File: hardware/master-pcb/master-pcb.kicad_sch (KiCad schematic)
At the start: 56 parts, among them J1 RS-485 OUT, J2 INT IN 0-8, J4 UNDERGLOW OUT, SW1 PLAYER_ID, U1 Teensy 4.0, U2 THVD1429, U3 SN74AHCT125

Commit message: Harness rework: INT twisted pair on JST XH, RS-485 shield on Micro-Fit pin 3
Two cabling changes, both of which replace earlier decisions.

INT goes twisted pair (signal + dedicated GND return)
-----------------------------------------------------
The panel side needed no change: J9 pin 2 was provisioned as GND for
exactly this on 2026-07-24. On the master, the 9-position pluggable
Euroblock is replaced by nine JST XH 2-pin vertical headers (B2B-XH-A),
placed as J2, J3, J5-J11 -- non-contiguous because renumbering J4 would
churn the docs for no gain.

Nine discrete 5.08mm screw blocks were rejected outright: ~92mm of board
edge against a 77.5mm board. XH is top-entry, so it needs no board edge
at all and the nine fit in roughly what the Euroblock vacated (~42x13.5
vs 45.72x12.0mm). XH is also keyed, so signal and GND cannot be swapped
at assembly -- that swap on a screw terminal ties INT to GND and reads as
a permanently stuck press. Keeping XH here while panel FSRs stay PH also
means an FSR lead cannot be plugged into an INT header.

Cost accepted: nine plugs instead of one detachable block.

Connectors are silkscreened by panel position (UL/U/UR/L/C/R/DL/D/DR),
left to right in panel order 0->8. This supersedes the old "J2 position 1
is panel 8" reversal note -- the mapping is now monotonic.

RS-485 shield terminated on pin 3
---------------------------------
Reverses the 2026-07-24 "drain floating at both ends" decision. That
reasoning was sound on its own terms; this takes the upgrade path the
old note itself described as a five-minute change.

Hybrid grounding, one continuous shield master -> panel 8:
  - master J1 pin 3 -> GND, the single DC reference for the network
  - each panel: RS485_Shield passes J8.3 -> J10.3, no local GND tie,
    plus C57 100nF || R20 1M to GND near J8

The per-panel caps are not decoration: ~6-8m of foil grounded at one end
only resonates near 10MHz, inside 1Mbps harmonic content. The cap grounds
it at RF while blocking DC, so no loo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
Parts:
- removed J2: INT IN 0-8, master-pcb:TerminalBlock_Molex_39531_1x09_P5.08mm_Vertical, symbol Connector_Generic:Conn_01x09
- added J10, J11, J2, J3, J5, J6, J7, J8, J9: B2B-XH-A, Connector_JST:JST_XH_B2B-XH-A_1x02_P2.50mm_Vertical, symbol Connector_Generic:Conn_01x02
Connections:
- net GND: now also J1.3 (Pin_3), J10.2 (Pin_2), J11.2 (Pin_2), J2.2 (Pin_2), J3.2 (Pin_2), J5.2 (Pin_2), J6.2 (Pin_2), J7.2 (Pin_2), J8.2 (Pin_2), J9.2 (Pin_2)
- net at D4.1 (K), R8.1: now also J5.1 (Pin_1)
- net at D2.1 (K), R6.1: now also J2.1 (Pin_1)
- net at D3.1 (K), R7.1: now also J3.1 (Pin_1)
- net at D10.1 (K), R14.1: now also J11.1 (Pin_1)
- net at D8.1 (K), R12.1: now also J9.1 (Pin_1)
- net at D5.1 (K), R9.1: now also J6.1 (Pin_1)
- net at D6.1 (K), R10.1: now also J7.1 (Pin_1)
- net at D7.1 (K), R11.1: now also J8.1 (Pin_1)
- net at D9.1 (K), R13.1: now also J10.1 (Pin_1)
- no-connect marks 12 -> 11
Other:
- note added: "*Shield"

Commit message: master: renumber reference designators contiguously from 1
The review conventions ask that each RefDes type start at 1 with no
numeric gaps. This board was missing D1 and R2. Reannotated, then pushed
through to the layout.

DRC 0, unconnected 0, schematic parity 0, ERC 0 with zones refilled.
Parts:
- renumbered C4 to C10, C3 to C11, C11 to C3, C10 to C4, C9 to C5, C8 to C6, C6 to C8, C5 to C9, D10 to D1, D9 to D2, D8 to D3, D7 to D4, D6 to D5, D5 to D6, D4 to D7, D3 to D8, D2 to D9, H3 to H2, H2 to H3, J4 to J2, J2 to J3, J3 to J4, R4 to R1, R9 to R11, R8 to R12, R7 to R13, R6 to R14, R5 to R2, R1 to R3, R15 to R4, R3 to R5, R14 to R6, R13 to R7, R12 to R8, R11 to R9, TP9 to TP1, TP8 to TP10, TP3 to TP2, TP10 to TP3, TP5 to TP4, TP6 to TP5, TP4 to TP6, TP1 to TP7, TP2 to TP8, TP7 to TP9, U2 to U1, U1 to U2

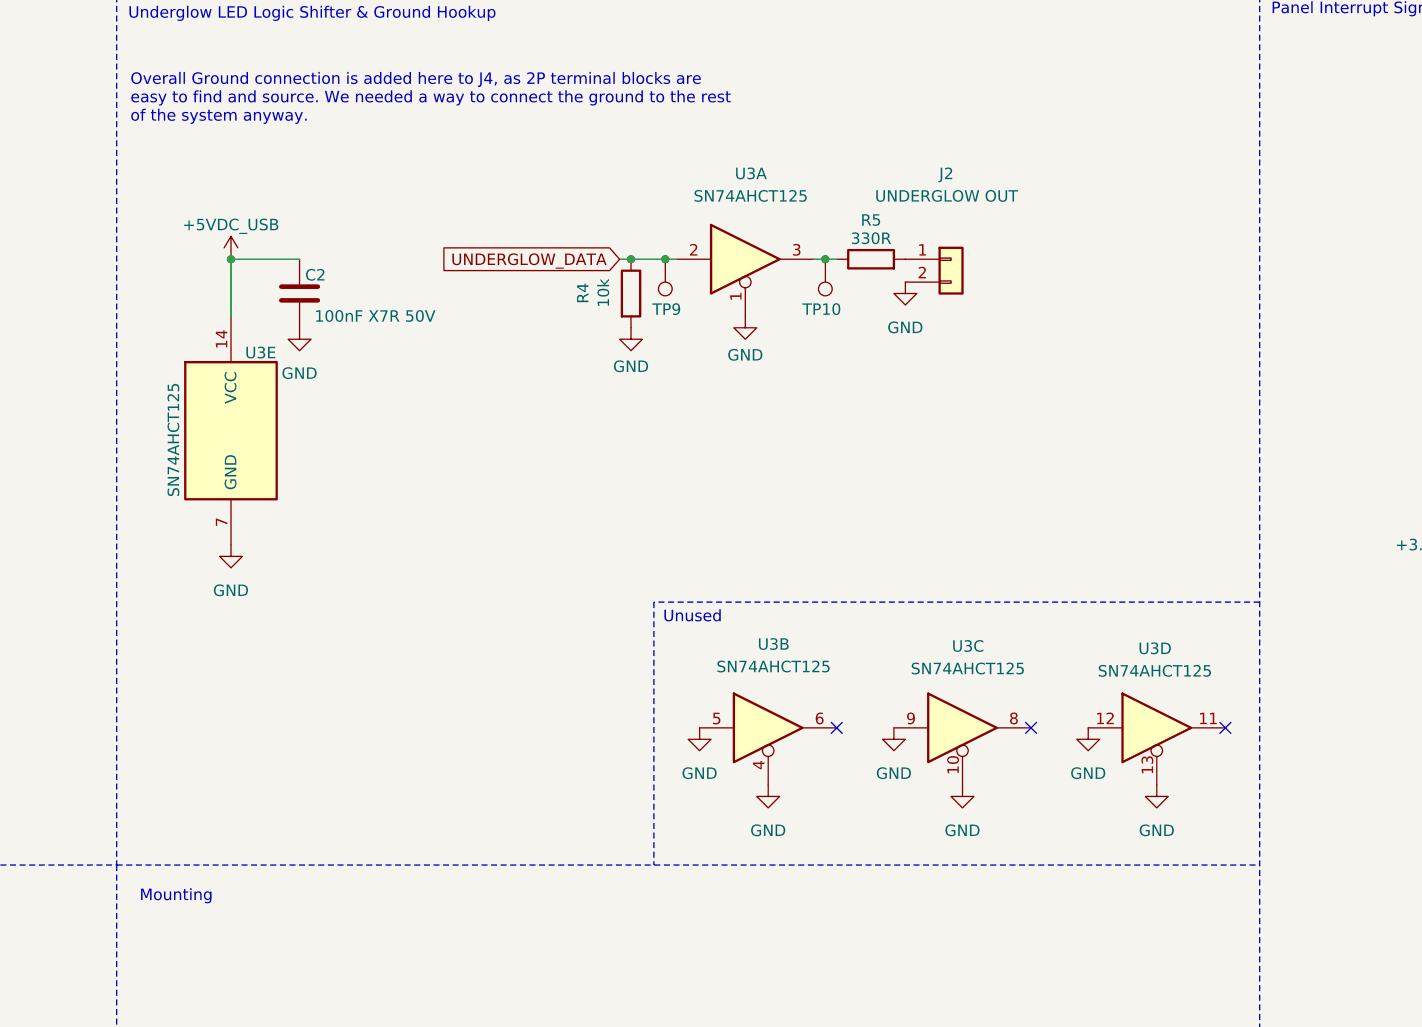
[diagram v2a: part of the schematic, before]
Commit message: shifter: swap quad SN74AHCT125 for single-gate SN74AHCT1G125 on all boards
External review suggested 74LVC1G34/74LVC1G17 since only one gate was used;
LVC was rejected on input thresholds (VIH = 0.7*VCC = 3.5V at 5V; the 1G17's
Schmitt VT+ max hits 3.33V at 5.5V) but the single-gate idea was right.
SN74AHCT1G125DBVR keeps AHCT's guaranteed TTL VIH of 2.0V in a SOT-23-5:
LCSC C7484, DigiKey 296-4708-1-ND. OE tied to GND; decoupling caps kept.

- panel-pcb U4, dual-panel brain U301, master-pcb U3: schematic symbol,
  footprint, placement and routing redone; spare-gate GND ties and
  no-connects removed
- panel: +5V feed re-routed with a short B.Cu hop under the LED_DATA riser
- master: DIP-14 replaced by SMD; new via drops the B.Cu underglow trace
  onto the A pad, new GND via feeds the OE pad's thermal spokes
- docs + BOMs updated (CLAUDE.md, PANEL_PCB, MASTER_PCB, BOM, UNDERGLOW,
  PRE_ORDER_CHECKLIST, dual-panel README, master-pcb-BOM.csv)

Verification: ERC 0 on all three projects; DRC 0 on panel and master;
dual-panel at its expected floor (19 cross-gap airwires, 90 pre-existing
PWR_FLAG parity conflicts, down from 92).
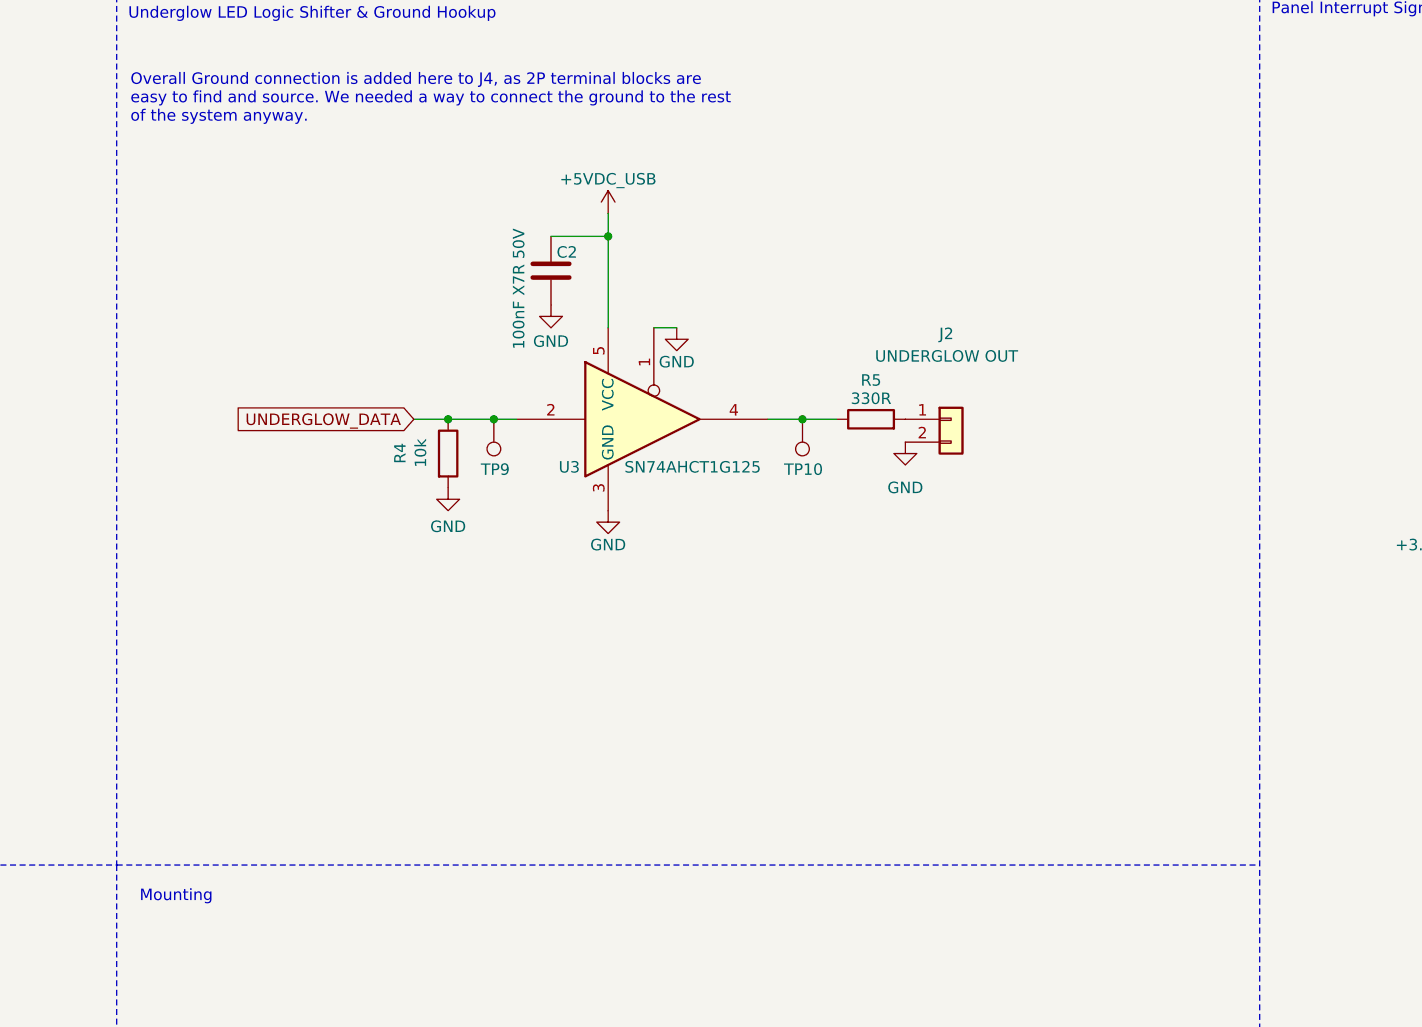
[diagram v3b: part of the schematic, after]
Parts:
- removed U3: SN74AHCT125, Package_DIP:DIP-14_W7.62mm, symbol 74xx:74AHCT125
- added U3: SN74AHCT1G125, Package_TO_SOT_SMD:SOT-23-5, symbol 74xGxx:74AHCT1G125
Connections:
- net +5VDC_USB: now also U3.5 (VCC)
- net GND: now also U3.1, U3.3 (GND)
- net UNDERGLOW_DATA: now also U3.2
- net at R5.1, TP10.1: now also U3.4
- no-connect marks 11 -> 8
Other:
- note removed: "Unused"
- moved on the sheet: C2, J2, R4, R5, TP10, TP9

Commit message: rev1: order both boards, and freeze exactly what went to fab
Boards are at JLCPCB as of 2026-08-18. Everything after this commit is rev 2.

Four design changes made on order day, all verified before submitting:

- U306 RP2040 signal pads 0.20 -> 0.23 mm, matching Raspberry Pi's official
  land pattern, via a local footprint. Length/pitch/centres/EP unchanged.
  Needed a zone refill and scoping the QSPI pour rule to B.Type == 'Zone'
  (it had no B-side condition, so it was policing track-to-pad too).
- RS-485 transceiver THVD1429 -> THVD1450DR on BOTH boards. Identical SOIC-8
  pinout. Gives up on-die IEC 61000-4-5 surge, which TI scopes to lightning and
  power-grid transients; gains 18 kV vs 8 kV contact ESD, the threat this pad
  actually documents. Also -$52 and 84x the stock, retiring the BOM's tightest
  line (60 units).
- 10 nF ADC filter caps C57112 -> C723749. The old part was X7R while the
  schematic said C0G; these are the four FSR ADC inputs, where Class II's
  piezoelectric response would inject charge synchronously with a footstep.
  Found by auditing all 35 BOM lines against live LCSC pages.
- master-pcb: 297 vias 0.45 -> 0.60 mm (0.075 -> 0.150 mm annular), after
  running DFM on the master for the first time. A quote is not a DFM check.

Both boards re-verified after every change: dual-panel 0/19/90/0,
master 0/0/0/0.

Adds hardware/fab-archive/rev1-2026-08-18/ with the byte-exact artifacts that
were manufactured, plus SHA256SUMS and a .gitattributes that disables CRLF
normalisation so they stay byte-exact. hardware/**/production/ is gitignored,
so without this there would be no record in git of what was physically built.

Adds QUOTE-2026-08-18.md (the real qty-20 quote; the July one is now marked
superseded) and splits the JLC order notes into PCB and PCBA remark blocks,
each within the 500-character limit the order form imposes.
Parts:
- U1: value THVD1429 -> THVD1450; LCSC C1850236 -> C2671361; MPN THVD1429DR -> THVD1450DR
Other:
- note added: "RS-485 bias (R4/R5): fitted as DNP footprints, insurance only. THVD1450 has integrated open/short/idle failsafe, so the idle bus is already defined and no external bias is normally needed. Bias belongs at ONE point on the bus - the master is that point, so if the bench ever disagrees, populate here and nowhere else. 390R pair = approx. 236mV across the 60R terminated bus at 3.3V."
- note removed: "RS-485 bias (R4/R5): fitted as DNP footprints, insurance only. THVD1429 has integrated open/short/idle failsafe, so the idle bus is already defined and no external bias is normally needed. Bias belongs at ONE point on the bus - the master is that point, so if the bench ever disagrees, populate here and nowhere else. 390R pair = approx. 236mV across the 60R terminated bus at 3.3V."
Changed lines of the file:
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@@
 		)
 	)
-	(text "RS-485 bias (R4/R5): fitted as DNP footprints, insurance only.\nTHVD1429 has integrated open/short/idle failsafe, so the idle bus\nis already defined and no external bias is normally needed.\nBias belongs at ONE point on the bus - the master is that point,\nso if the bench ever disagrees, populate here and nowhere else.\n390R pair = approx. 236mV across the 60R terminated bus at 3.3V."
+	(text "RS-485 bias (R4/R5): fitted as DNP footprints, insurance only.\nTHVD1450 has integrated open/short/idle failsafe, so the idle bus\nis already defined and no external bias is normally needed.\nBias belongs at ONE point on the bus - the master is that point,\nso if the bench ever disagrees, populate here and nowhere else.\n390R pair = approx. 236mV across the 60R terminated bus at 3.3V."
 		(exclude_from_sim no)
 		(at 14.224 122.936 0)
@@
 			)
 		)
-		(property "Description" "DNP failsafe bias insurance (panel review 3.a, 2026-07-20): pull-up RS485+ (A) to +3V3. THVD1429 integrated open/short/idle failsafe makes bias normally unnecessary; populate R4+R5 only if idle-bus noise is ever observed. 390R pair gives ~236mV across 60R differential load at 3.3V. PARKED UNWIRED - to be wired DNP by hand."
+		(property "Description" "DNP failsafe bias insurance (panel review 3.a, 2026-07-20): pull-up RS485+ (A) to +3V3. THVD1450 integrated open/short/idle failsafe makes bias normally unnecessary; populate R4+R5 only if idle-bus noise is ever observed. 390R pair gives ~236mV across 60R differential load at 3.3V. PARKED UNWIRED - to be wired DNP by hand."
 			(at 88.9 161.29 0)
 			(hide yes)
@@
 			)
 		)
-		(property "Value" "THVD1429"
+		(property "Value" "THVD1450"
 			(at 78.994 180.594 90)
 			(show_name no)
@@
 			)
 		)
-		(property "Datasheet" "https://www.ti.com/lit/ds/symlink/thvd1429.pdf"
+		(property "Datasheet" "https://www.ti.com/lit/ds/symlink/thvd1450.pdf"
 			(at 70.3 172.87 0)
 			(hide yes)
@@
 			)
 		)
-		(property "LCSC" "C1850236"
+		(property "LCSC" "C2671361"
 			(at 70.3 172.87 0)
 			(hide yes)
@@
 			)
 		)
-		(property "MPN" "THVD1429DR"
+		(property "MPN" "THVD1450DR"
 			(at 70.3 172.87 0)
 			(hide yes)
